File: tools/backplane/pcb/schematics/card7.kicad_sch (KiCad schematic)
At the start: 3 parts

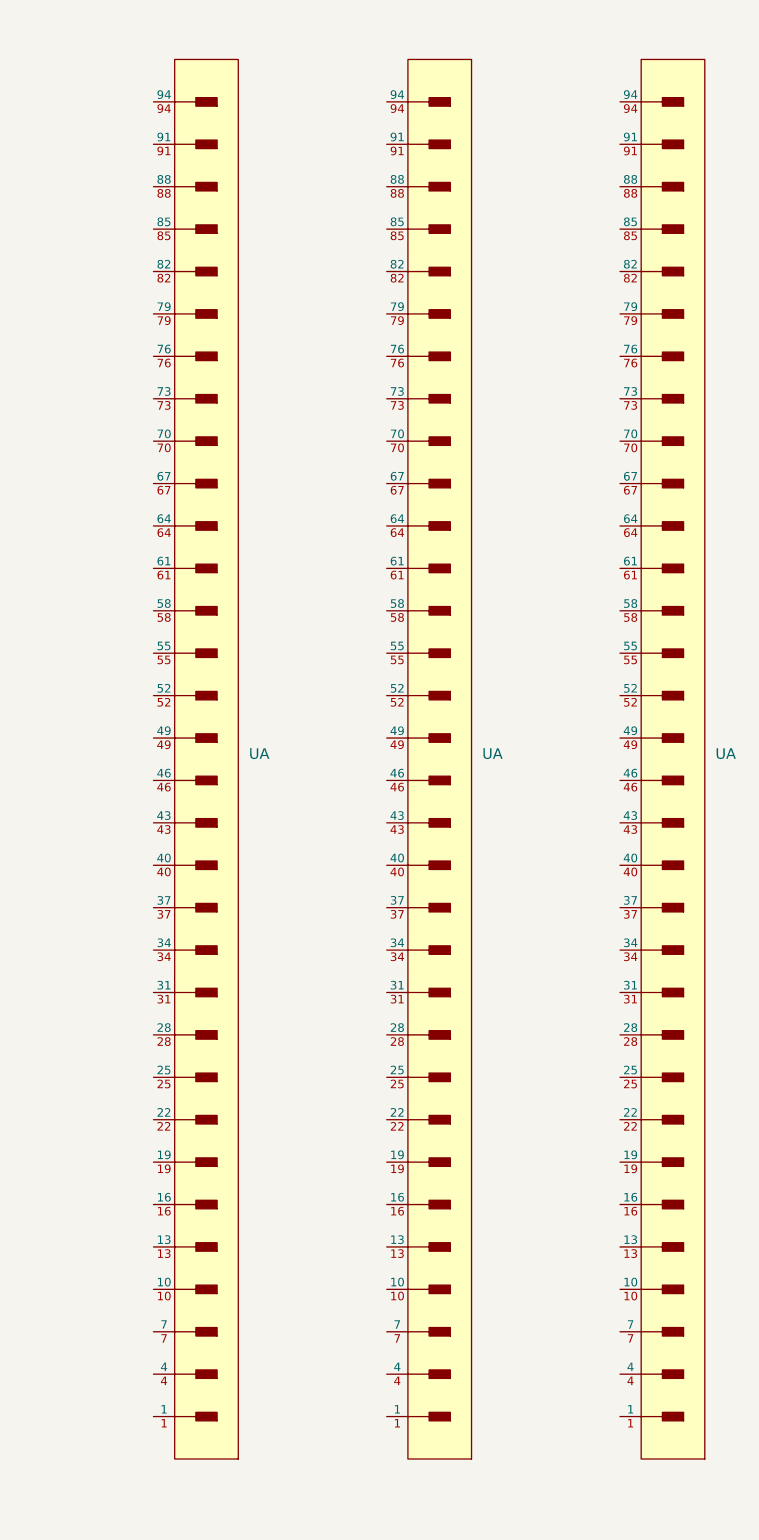
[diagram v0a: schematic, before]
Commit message: start routing the backplane
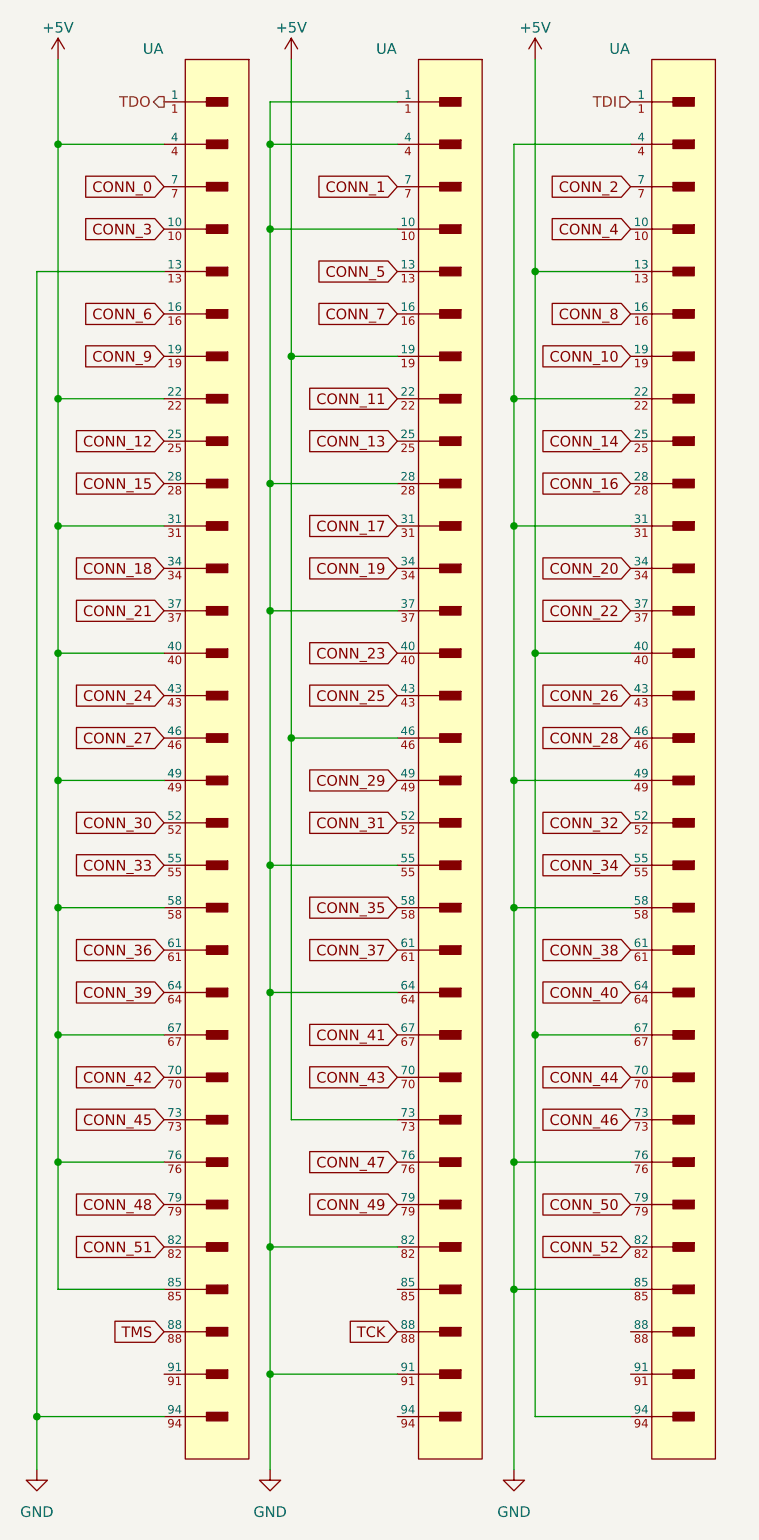
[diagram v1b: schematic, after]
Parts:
- removed U (x3): (no value), symbol 09032967825:09032967825
- added U (x3): (no value), symbol 09032967825:09032967825
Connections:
- new net +5V: U.13, U.19, U.22, U.31, U.4, U.40, U.40, U.46, U.49, U.58, U.67, U.67, U.73, U.76, U.85, U.94
- new net CONN_0: U.7
- new net CONN_1: U.7
- new net CONN_10: U.19
- new net CONN_11: U.22
- new net CONN_12: U.25
- new net CONN_13: U.25
- new net CONN_14: U.25
- new net CONN_15: U.28
- new net CONN_16: U.28
- new net CONN_17: U.31
- new net CONN_18: U.34
- new net CONN_19: U.34
- new net CONN_2: U.7
- new net CONN_20: U.34
- new net CONN_21: U.37
- new net CONN_22: U.37
- new net CONN_23: U.40
- new net CONN_24: U.43
- new net CONN_25: U.43
- new net CONN_26: U.43
- new net CONN_27: U.46
- new net CONN_28: U.46
- new net CONN_29: U.49
- new net CONN_3: U.10
- new net CONN_30: U.52
- new net CONN_31: U.52
- new net CONN_32: U.52
- new net CONN_33: U.55
- new net CONN_34: U.55
- new net CONN_35: U.58
- new net CONN_36: U.61
- new net CONN_37: U.61
- new net CONN_38: U.61
- new net CONN_39: U.64
- new net CONN_4: U.10
- new net CONN_40: U.64
- new net CONN_41: U.67
- new net CONN_42: U.70
- new net CONN_43: U.70
- new net CONN_44: U.70
- new net CONN_45: U.73
- new net CONN_46: U.73
- new net CONN_47: U.76
- new net CONN_48: U.79
- new net CONN_49: U.79
- new net CONN_5: U.13
- new net CONN_50: U.79
- new net CONN_51: U.82
- new net CONN_52: U.82
- new net CONN_6: U.16
- new net CONN_7: U.16
- new net CONN_8: U.16
- new net CONN_9: U.19
- new net GND: U.1, U.10, U.13, U.22, U.28, U.31, U.37, U.4, U.4, U.49, U.55, U.58, U.64, U.76, U.82, U.85, U.91, U.94
- new net TCK: U.88
- new net TDI: U.1
- new net TDO: U.1
- new net TMS: U.88
